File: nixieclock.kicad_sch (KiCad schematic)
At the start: 34 parts, among them Q1 MMBTA42, Q2 FDS2672CT, U1 UCC3803

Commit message: things happened
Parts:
- added NX1, NX2, NX3, NX4, NX5, NX6: IN-12A, nixies-us:nixies-us-IN-12, symbol nixies-us:IN-12A
- added TP1, TP2, TP3: TestPoint_Probe, TestPoint:TestPoint_Pad_2.0x2.0mm, symbol Connector:TestPoint_Probe
- added U2: K155NA1, symbol k155Id1:K155NA1
- added U3: PicoW, RPi_PicoW:RPi_Pico_SMD_TH, symbol RPi_Pico:PicoW
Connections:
- net +5V: now also TP1.1
- net GND: now also TP3.1, U2.12 (GND), U3.3 (GND)
- net +160V renamed +170V
- net +170V: now also TP2.1
- new net: NX1.8, U2.1 (8)
- new net: NX1.7, U2.10 (7)
- new net: NX1.6, U2.11 (6)
- new net: NX1.4, U2.13 (4)
- new net: NX1.5, U2.14 (5)
- new net: NX1.1, U2.15 (1)
- new net: NX1.0, U2.16 (0)
- new net: NX1.9, U2.2 (9)
- new net: NX1.2, U2.8 (2)
- new net: NX1.3, U2.9 (3)

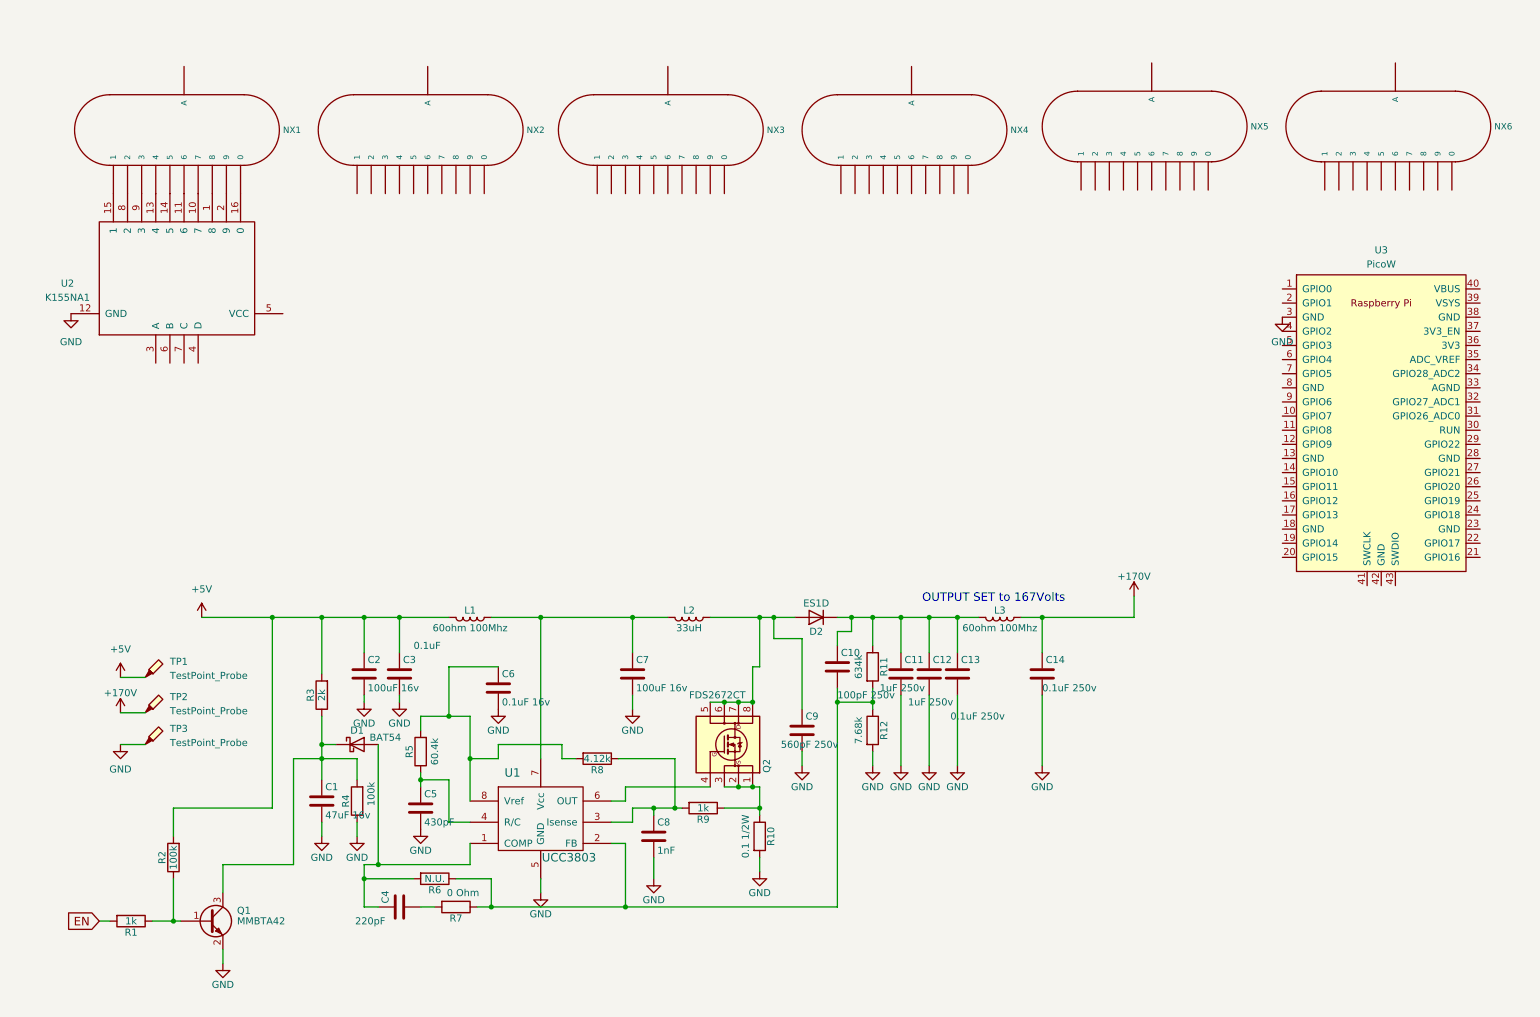
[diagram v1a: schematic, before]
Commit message: schematic mostly done, started laying out board
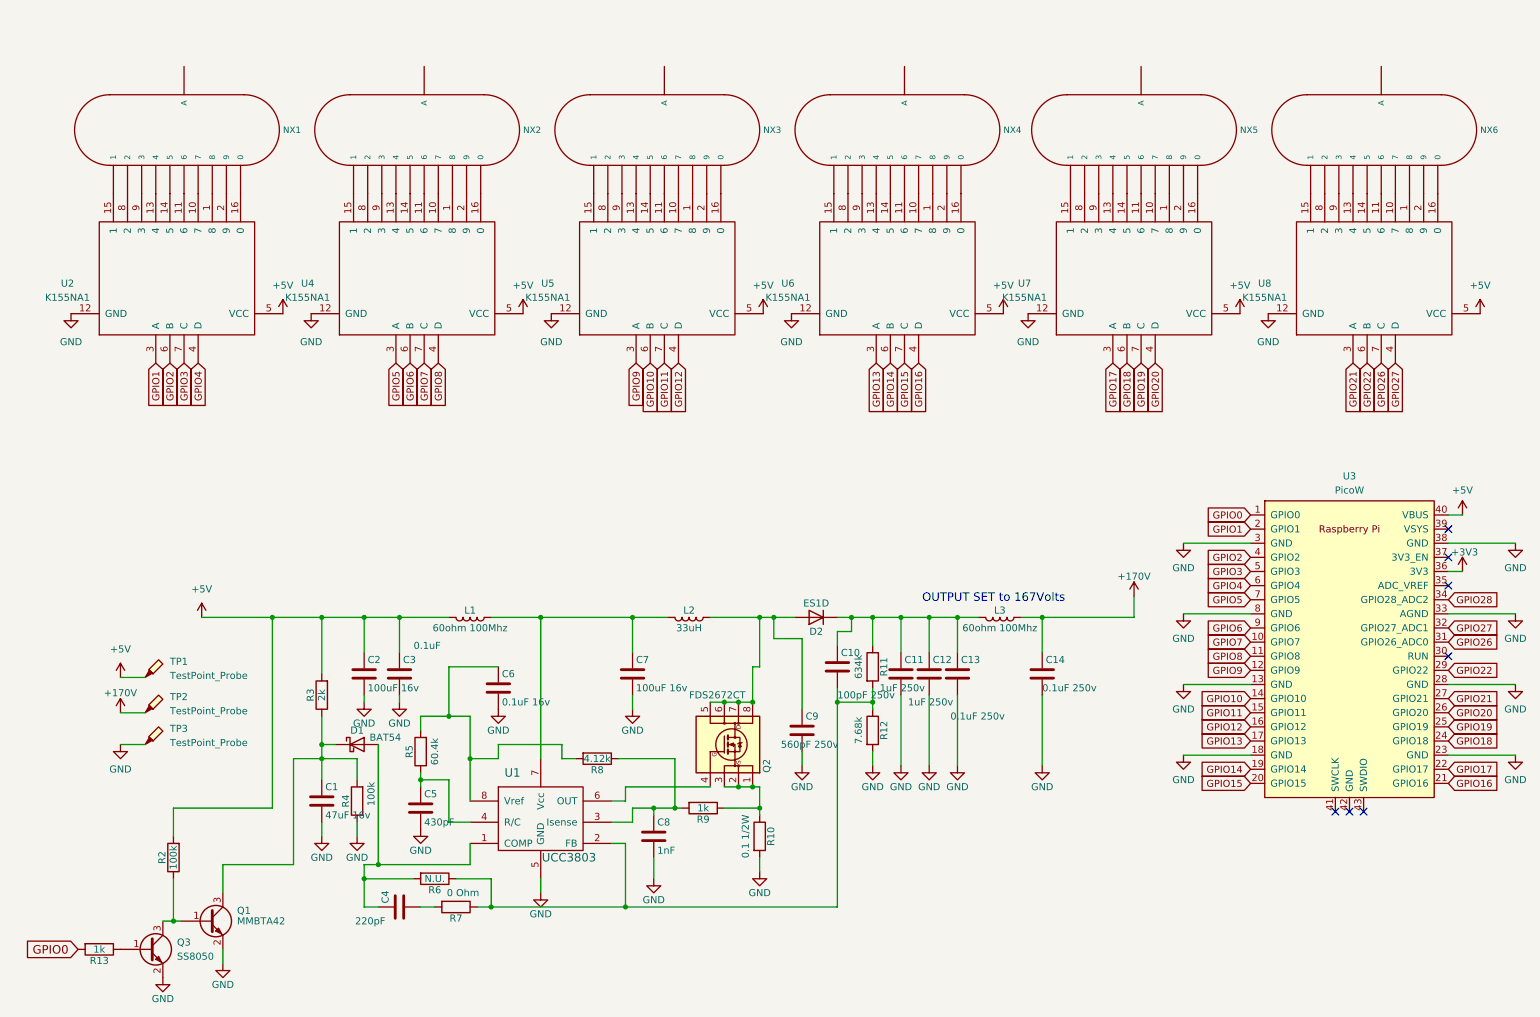
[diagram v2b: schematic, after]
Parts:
- removed R1: 1k, Resistor_SMD:R_0603_1608Metric_Pad0.98x0.95mm_HandSolder, symbol Device:R
- added Q3: SS8050, Package_TO_SOT_SMD:SOT-23, symbol Transistor_BJT:SS8050
- added R13: 1k, Resistor_SMD:R_0603_1608Metric_Pad0.98x0.95mm_HandSolder, symbol Device:R
- added U4, U5, U6, U7, U8: K155NA1, Package_DIP:DIP-16_W7.62mm_LongPads, symbol k155Id1:K155NA1
- U2: footprint (none) -> Package_DIP:DIP-16_W7.62mm_LongPads
- U3: footprint RPi_PicoW:RPi_Pico_SMD_TH -> RPi_Pico:RPi_PicoW_SMD_TH
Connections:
- net +5V: now also U2.5 (VCC), U3.40 (VBUS), U4.5 (VCC), U5.5 (VCC), U6.5 (VCC), U7.5 (VCC), U8.5 (VCC)
- net GND: now also U3.13 (GND), U3.18 (GND), U3.23 (GND), U3.28 (GND), U3.33 (AGND), U3.38 (GND), U3.8 (GND), Q3.2 (E), U4.12 (GND), U5.12 (GND), U6.12 (GND), U7.12 (GND), U8.12 (GND)
- net at NX6.0: now also U8.16 (0)
- net at NX6.1: now also U8.15 (1)
- net at NX6.2: now also U8.8 (2)
- net at NX6.3: now also U8.9 (3)
- net at NX6.4: now also U8.13 (4)
- net at NX6.5: now also U8.14 (5)
- net at NX6.6: now also U8.11 (6)
- net at NX6.7: now also U8.10 (7)
- net at NX6.8: now also U8.1 (8)
- net at NX6.9: now also U8.2 (9)
- net at NX2.0: now also U4.16 (0)
- net at NX2.1: now also U4.15 (1)
- net at NX2.2: now also U4.8 (2)
- net at NX2.3: now also U4.9 (3)
- net at NX2.4: now also U4.13 (4)
- net at NX2.5: now also U4.14 (5)
- net at NX2.6: now also U4.11 (6)
- net at NX2.7: now also U4.10 (7)
- net at NX2.8: now also U4.1 (8)
- net at NX2.9: now also U4.2 (9)
- net at Q1.1 (B), R2.1: now also Q3.3 (C)
- net GPIO1: now reaches U2.3 (A)
- net GPIO1: now also U3.2 (GPIO1)
- net GPIO4: now reaches U2.4 (D)
- net GPIO4: now also U3.6 (GPIO4)
- net GPIO2: now reaches U2.6 (B)
- net GPIO2: now also U3.4 (GPIO2)
- net GPIO3: now reaches U2.7 (C)
- net GPIO3: now also U3.5 (GPIO3)
- net at NX4.0: now also U6.16 (0)
- net at NX4.1: now also U6.15 (1)
- net at NX4.2: now also U6.8 (2)
- net at NX4.3: now also U6.9 (3)
- net at NX4.4: now also U6.13 (4)
- net at NX4.5: now also U6.14 (5)
- net at NX4.6: now also U6.11 (6)
- net at NX4.7: now also U6.10 (7)
- net at NX4.8: now also U6.1 (8)
- net at NX4.9: now also U6.2 (9)
- net GPIO0: now reaches U3.1 (GPIO0)
- net GPIO0: now also R13.2
- net GPIO7: now reaches U3.10 (GPIO7)
- net GPIO7: now also U4.7 (C)
- net GPIO8: now reaches U3.11 (GPIO8)
- net GPIO8: now also U4.4 (D)
- net GPIO9: now reaches U3.12 (GPIO9)
- net GPIO9: now also U5.3 (A)
- net GPIO10: now reaches U3.14 (GPIO10)
- net GPIO10: now also U5.6 (B)
- net GPIO11: now reaches U3.15 (GPIO11)
- net GPIO11: now also U5.7 (C)
- net GPIO12: now reaches U3.16 (GPIO12)
- net GPIO12: now also U5.4 (D)
- net GPIO13: now reaches U3.17 (GPIO13)
- net GPIO13: now also U6.3 (A)
- net GPIO14: now reaches U3.19 (GPIO14)
- net GPIO14: now also U6.6 (B)
- net GPIO15: now reaches U3.20 (GPIO15)
- net GPIO15: now also U6.7 (C)
- net GPIO16: now reaches U3.21 (GPIO16)
- net GPIO16: now also U6.4 (D)
- net GPIO17: now reaches U3.22 (GPIO17)
- net GPIO17: now also U7.3 (A)
- net GPIO18: now reaches U3.24 (GPIO18)
- net GPIO18: now also U7.6 (B)
- net GPIO19: now reaches U3.25 (GPIO19)
- net GPIO19: now also U7.7 (C)
- net GPIO20: now reaches U3.26 (GPIO20)
- net GPIO20: now also U7.4 (D)
- net GPIO21: now reaches U3.27 (GPIO21)
- net GPIO21: now also U8.3 (A)
- net GPIO22: now reaches U3.29 (GPIO22)
- net GPIO22: now also U8.6 (B)
- net GPIO26: now reaches U3.31 (GPIO26_ADC0)
- net GPIO26: now also U8.7 (C)
- net GPIO27: now reaches U3.32 (GPIO27_ADC1)
- net GPIO27: now also U8.4 (D)
- net GPIO28: now reaches U3.34 (GPIO28_ADC2)
- net +3V3: now reaches U3.36 (3V3)
- net GPIO5: now reaches U3.7 (GPIO5)
- net GPIO5: now also U4.3 (A)
- net GPIO6: now reaches U3.9 (GPIO6)
- net GPIO6: now also U4.6 (B)
- net at NX5.0: now also U7.16 (0)
- net at NX5.1: now also U7.15 (1)
- net at NX5.2: now also U7.8 (2)
- net at NX5.3: now also U7.9 (3)
- net at NX5.4: now also U7.13 (4)
- net at NX5.5: now also U7.14 (5)
- net at NX5.6: now also U7.11 (6)
- net at NX5.7: now also U7.10 (7)
- net at NX5.8: now also U7.1 (8)
- net at NX5.9: now also U7.2 (9)
- net at NX3.0: now also U5.16 (0)
- net at NX3.1: now also U5.15 (1)
- net at NX3.2: now also U5.8 (2)
- net at NX3.3: now also U5.9 (3)
- net at NX3.4: now also U5.13 (4)
- net at NX3.5: now also U5.14 (5)
- net at NX3.6: now also U5.11 (6)
- net at NX3.7: now also U5.10 (7)
- net at NX3.8: now also U5.1 (8)
- net at NX3.9: now also U5.2 (9)
- new net: Q3.1 (B), R13.1
- no-connect marks 0 -> 7
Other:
- moved on the sheet: U3

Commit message: mostly done i guess?
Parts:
- added R1, R14, R15, R16, R17, R18: 10.5k, Resistor_SMD:R_0805_2012Metric_Pad1.20x1.40mm_HandSolder, symbol Device:R_Small
- R11: footprint Resistor_SMD:R_0603_1608Metric_Pad0.98x0.95mm_HandSolder -> Resistor_SMD:R_1206_3216Metric_Pad1.30x1.75mm_HandSolder; LCSC Part C2999499 -> C3037408
- R12: footprint Resistor_SMD:R_0603_1608Metric_Pad0.98x0.95mm_HandSolder -> Resistor_SMD:R_1206_3216Metric_Pad1.30x1.75mm_HandSolder; LCSC Part C23102 -> C3037264
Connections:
- net +170V: now also R1.1, R14.1, R15.1, R16.1, R17.1, R18.1
- net at NX3.A: now also R15.2
- net at NX2.A: now also R14.2
- net at NX4.A: now also R16.2
- net at NX6.A: now also R18.2
- net at NX5.A: now also R17.2
- net at NX1.A: now also R1.2

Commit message: Finishing touches to pcb
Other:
- note added: "Power supply is from https://github.com/drkmsmithjr/NixiePowerSupply/tree/master/KC_NixieSupply5vTo170vMini"
- moved on the sheet: U2, U4, U5, U6, U7, U8

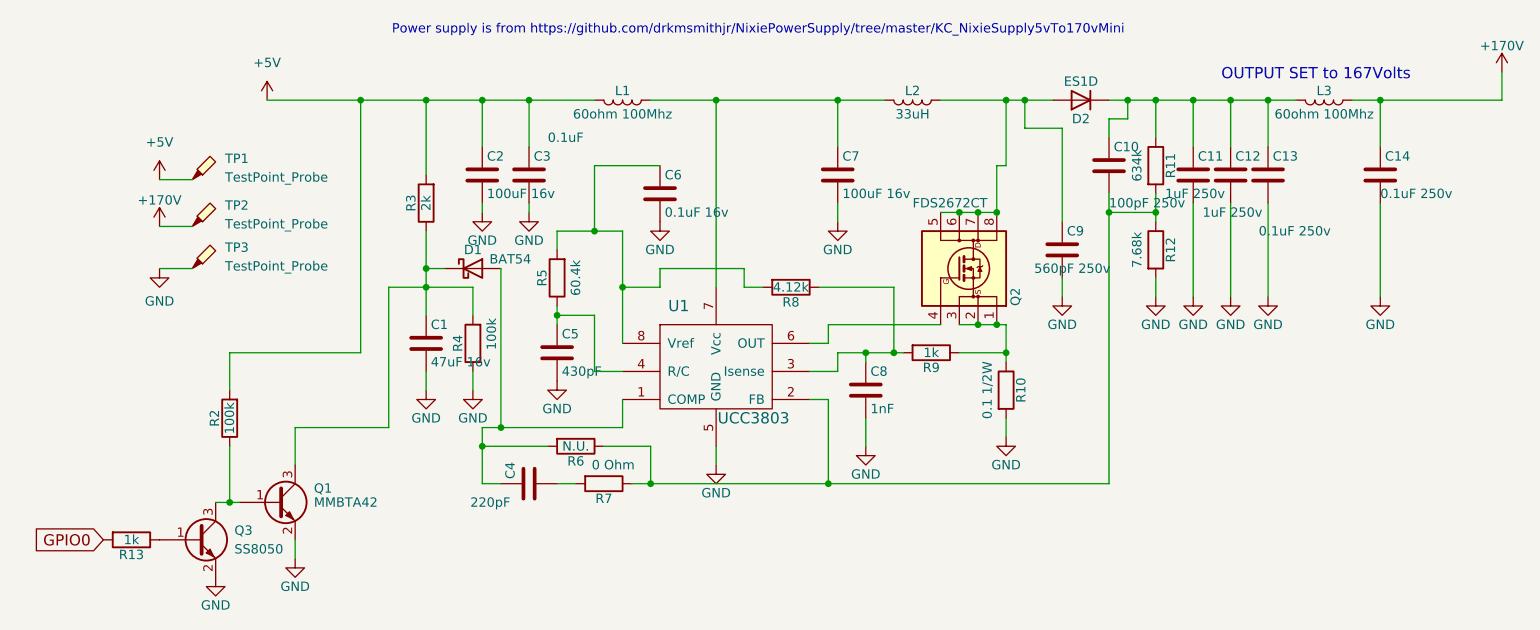
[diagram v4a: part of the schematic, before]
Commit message: updates to silk screen
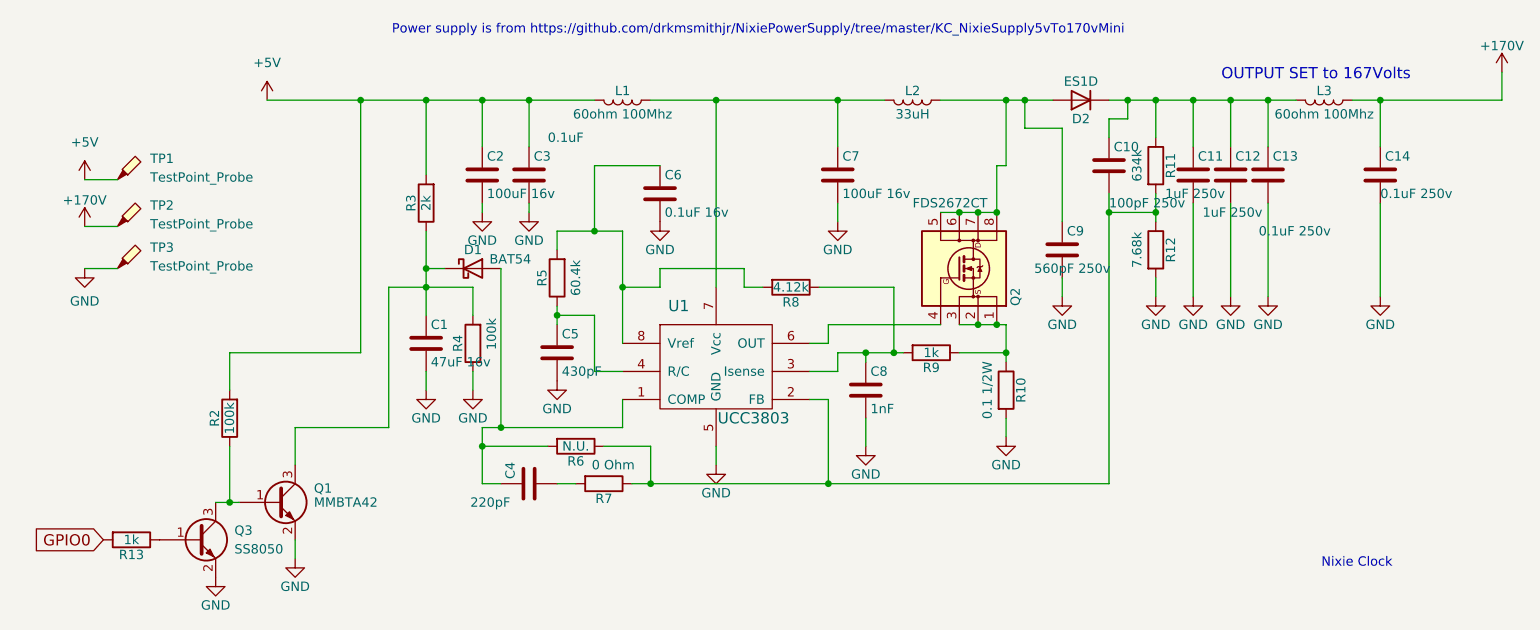
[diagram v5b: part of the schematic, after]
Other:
- note added: "Nixie Clock"
- moved on the sheet: TP1, TP2, TP3
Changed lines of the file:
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@@
 		)
 	)
+	(text "Nixie Clock"
+		(exclude_from_sim no)
+		(at 192.405 189.865 0)
+		(effects
+			(font
+				(face "FOT-Yuruka Std UB")
+				(size 1.27 1.27)
+				(color 0 0 255 1)
+			)
+		)
+	)
 	(text "OUTPUT SET to 167Volts"
 		(exclude_from_sim no)
@@
 	(wire
 		(pts
-			(xy 29.845 137.795) (xy 34.29 137.795)
+			(xy 19.685 137.795) (xy 24.13 137.795)
 		)
 		(stroke
@@
 	(wire
 		(pts
-			(xy 29.845 144.145) (xy 34.29 144.145)
+			(xy 19.685 144.145) (xy 24.13 144.145)
 		)
 		(stroke
@@
 	(wire
 		(pts
-			(xy 29.845 149.86) (xy 34.29 149.86)
+			(xy 19.685 149.86) (xy 24.13 149.86)
 		)
 		(stroke
@@
 	(symbol
 		(lib_id "Connector:TestPoint_Probe")
-		(at 34.29 137.795 0)
+		(at 24.13 137.795 0)
 		(unit 1)
 		(exclude_from_sim no)
@@
 		(fields_autoplaced yes)
 		(property "Reference" "TP1"
-			(at 38.735 134.9374 0)
+			(at 28.575 134.9374 0)
 			(effects
 				(font
@@
 		)
 		(property "Value" "TestPoint_Probe"
-			(at 38.735 137.4774 0)
+			(at 28.575 137.4774 0)
 			(effects
 				(font
@@
 		)
 		(property "Footprint" "TestPoint:TestPoint_Pad_2.0x2.0mm"
-			(at 39.37 137.795 0)
+			(at 29.21 137.795 0)
 			(effects
 				(font
@@
 		)
 		(property "Datasheet" "~"
-			(at 39.37 137.795 0)
+			(at 29.21 137.795 0)
 			(effects
 				(font
@@
 		)
 		(property "Description" "test point (alternative probe-style design)"
-			(at 34.29 137.795 0)
+			(at 24.13 137.795 0)
 			(effects
 				(font
@@
 	(symbol
 		(lib_id "Connector:TestPoint_Probe")
-		(at 34.29 149.86 0)
+		(at 24.13 149.86 0)
 		(unit 1)
 		(exclude_from_sim no)
@@
 		(fields_autoplaced yes)
 		(property "Reference" "TP3"
-			(at 38.735 147.0024 0)
+			(at 28.575 147.0024 0)
 			(effects
 				(font
@@
 		)
 		(property "Value" "TestPoint_Probe"
-			(at 38.735 149.5424 0)
+			(at 28.575 149.5424 0)
 			(effects
 				(font
@@
 		)
 		(property "Footprint" "TestPoint:TestPoint_Pad_2.0x2.0mm"
-			(at 39.37 149.86 0)
+			(at 29.21 149.86 0)
 			(effects
 				(font
@@
 		)
 		(property "Datasheet" "~"
-			(at 39.37 149.86 0)
+			(at 29.21 149.86 0)
 			(effects
 				(font
@@
 		)
 		(property "Description" "test point (alternative probe-style design)"
-			(at 34.29 149.86 0)
+			(at 24.13 149.86 0)
 			(effects
 				(font
@@
 	(symbol
 		(lib_id "power:GND")
-		(at 29.845 149.86 0)
+		(at 19.685 149.86 0)
 		(unit 1)
 		(exclude_from_sim no)
@@
 		(fields_autoplaced yes)
 		(property "Reference" "#PWR023"
-			(at 29.845 156.21 0)
+			(at 19.685 156.21 0)
 			(effects
 				(font
@@
 		)
 		(property "Value" "GND"
-			(at 29.845 154.305 0)
+			(at 19.685 154.305 0)
 			(effects
 				(font
@@
 		)
 		(property "Footprint" ""
-			(at 29.845 149.86 0)
+			(at 19.685 149.86 0)
 			(effects
 				(font
@@
 		)
 		(property "Datasheet" ""
-			(at 29.845 149.86 0)
+			(at 19.685 149.86 0)
 			(effects
 				(font
@@
 		)
 		(property "Description" "Power symbol creates a global label with name \"GND\" , ground"
-			(at 29.845 149.86 0)
+			(at 19.685 149.86 0)
 			(effects
 				(font
@@
 	(symbol
 		(lib_id "power:+5V")
-		(at 29.845 137.795 0)
+		(at 19.685 137.795 0)
 		(unit 1)
 		(exclude_from_sim no)
@@
 		(fields_autoplaced yes)
 		(property "Reference" "#PWR011"
-			(at 29.845 141.605 0)
+			(at 19.685 141.605 0)
 			(effects
 				(font
@@
 		)
 		(property "Value" "+5V"
-			(at 29.845 132.715 0)
+			(at 19.685 132.715 0)
 			(effects
 				(font
@@
 		)
 		(property "Footprint" ""
-			(at 29.845 137.795 0)
+			(at 19.685 137.795 0)
 			(effects
 				(font
@@
 		)
 		(property "Datasheet" ""
-			(at 29.845 137.795 0)
+			(at 19.685 137.795 0)
 			(effects
 				(font
@@
 		)
 		(property "Description" "Power symbol creates a global label with name \"+5V\""
-			(at 29.845 137.795 0)
+			(at 19.685 137.795 0)
 			(effects
 				(font
@@
 	(symbol
 		(lib_id "NixieSupply5vto170vDCMBoostMini-rescue:+160V")
-		(at 29.845 144.145 0)
+		(at 19.685 144.145 0)
 		(unit 1)
 		(exclude_from_sim no)
@@
 		(dnp no)
 		(property "Reference" "#PWR012"
-			(at 29.845 147.955 0)
+			(at 19.685 147.955 0)
 			(effects
 				(font
@@
 		)
 		(property "Value" "+170V"
-			(at 29.845 140.589 0)
+			(at 19.685 140.589 0)
 			(effects
 				(font
@@
 		)
 		(property "Footprint" ""
-			(at 29.845 144.145 0)
+			(at 19.685 144.145 0)
 			(effects
 				(font
@@
 		)
 		(property "Datasheet" ""
-			(at 29.845 144.145 0)
+			(at 19.685 144.145 0)
 			(effects
 				(font
@@
 		)
 		(property "Description" ""
-			(at 29.845 144.145 0)
+			(at 19.685 144.145 0)
 			(effects
 				(font
@@
 	(symbol
 		(lib_id "Connector:TestPoint_Probe")
-		(at 34.29 144.145 0)
+		(at 24.13 144.145 0)
 		(unit 1)
 		(exclude_from_sim no)
@@
 		(fields_autoplaced yes)
 		(property "Reference" "TP2"
-			(at 38.735 141.2874 0)
+			(at 28.575 141.2874 0)
 			(effects
 				(font
@@
 		)
 		(property "Value" "TestPoint_Probe"
-			(at 38.735 143.8274 0)
+			(at 28.575 143.8274 0)
 			(effects
 				(font
@@
 		)
 		(property "Footprint" "TestPoint:TestPoint_Pad_2.0x2.0mm"
-			(at 39.37 144.145 0)
+			(at 29.21 144.145 0)
 			(effects
 				(font
@@
 		)
 		(property "Datasheet" "~"
-			(at 39.37 144.145 0)
+			(at 29.21 144.145 0)
 			(effects
 				(font
@@
 		)
 		(property "Description" "test point (alternative probe-style design)"
-			(at 34.29 144.145 0)
+			(at 24.13 144.145 0)
 			(effects
 				(font
